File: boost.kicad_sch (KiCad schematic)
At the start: 41 parts, among them Q4 BSC059N04LS6, Q5 BSC059N04LS6, U17 LTC7804, U6 LTC7804

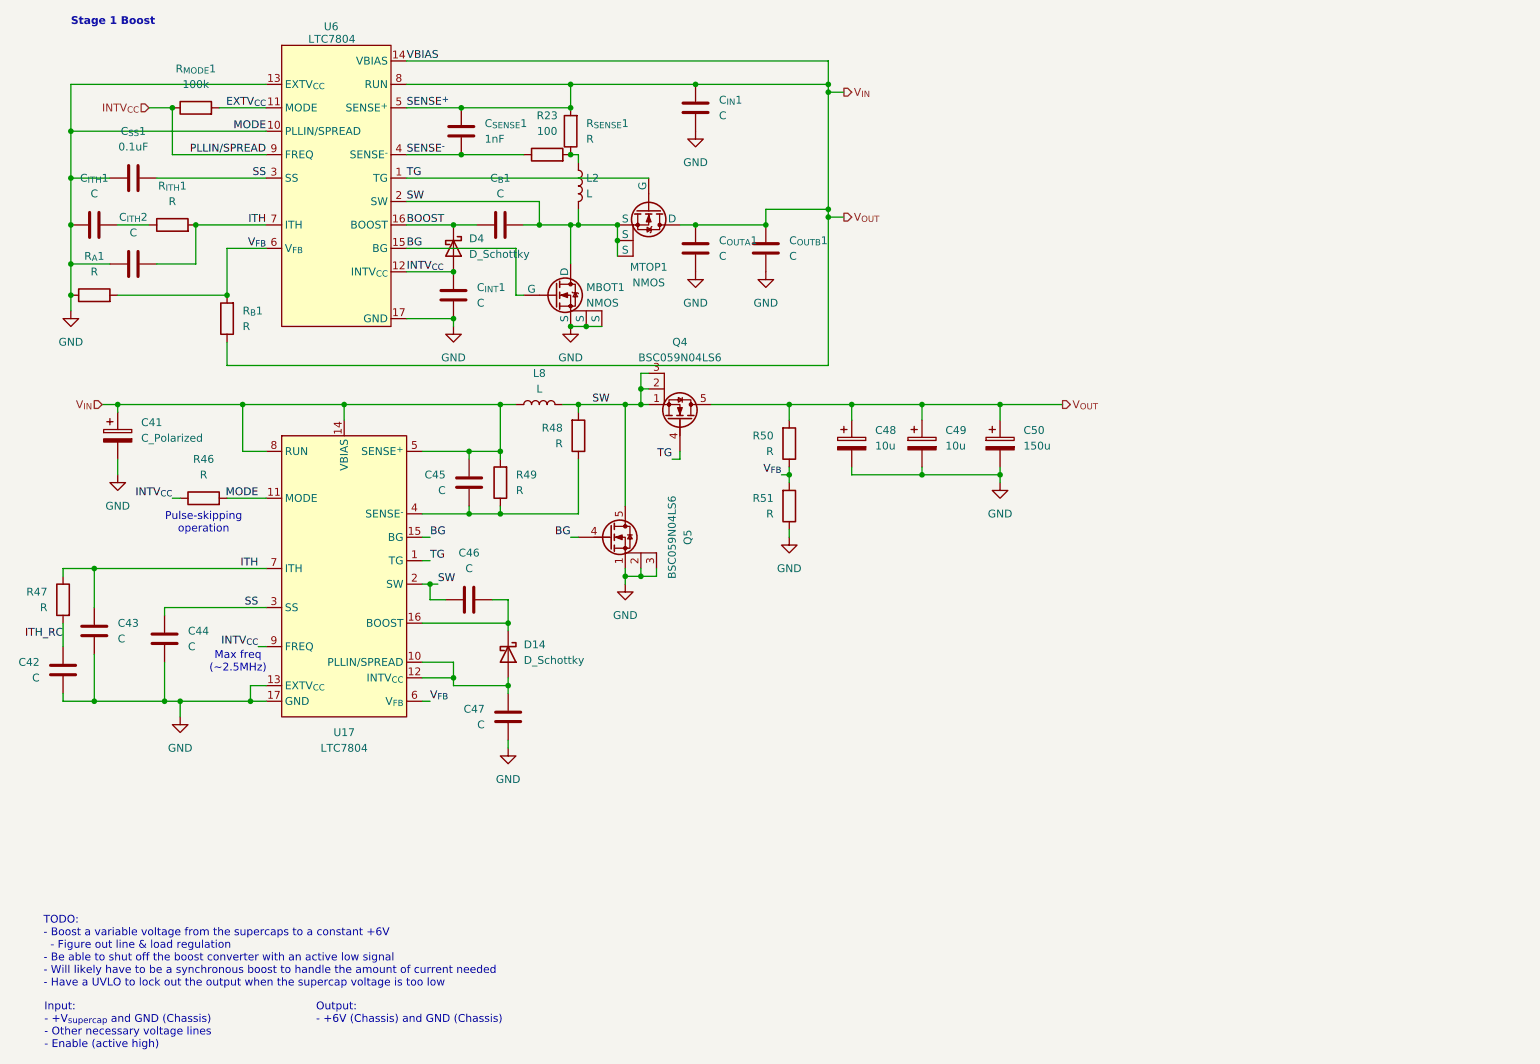
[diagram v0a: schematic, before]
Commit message: Redo boost converter (frist stage)
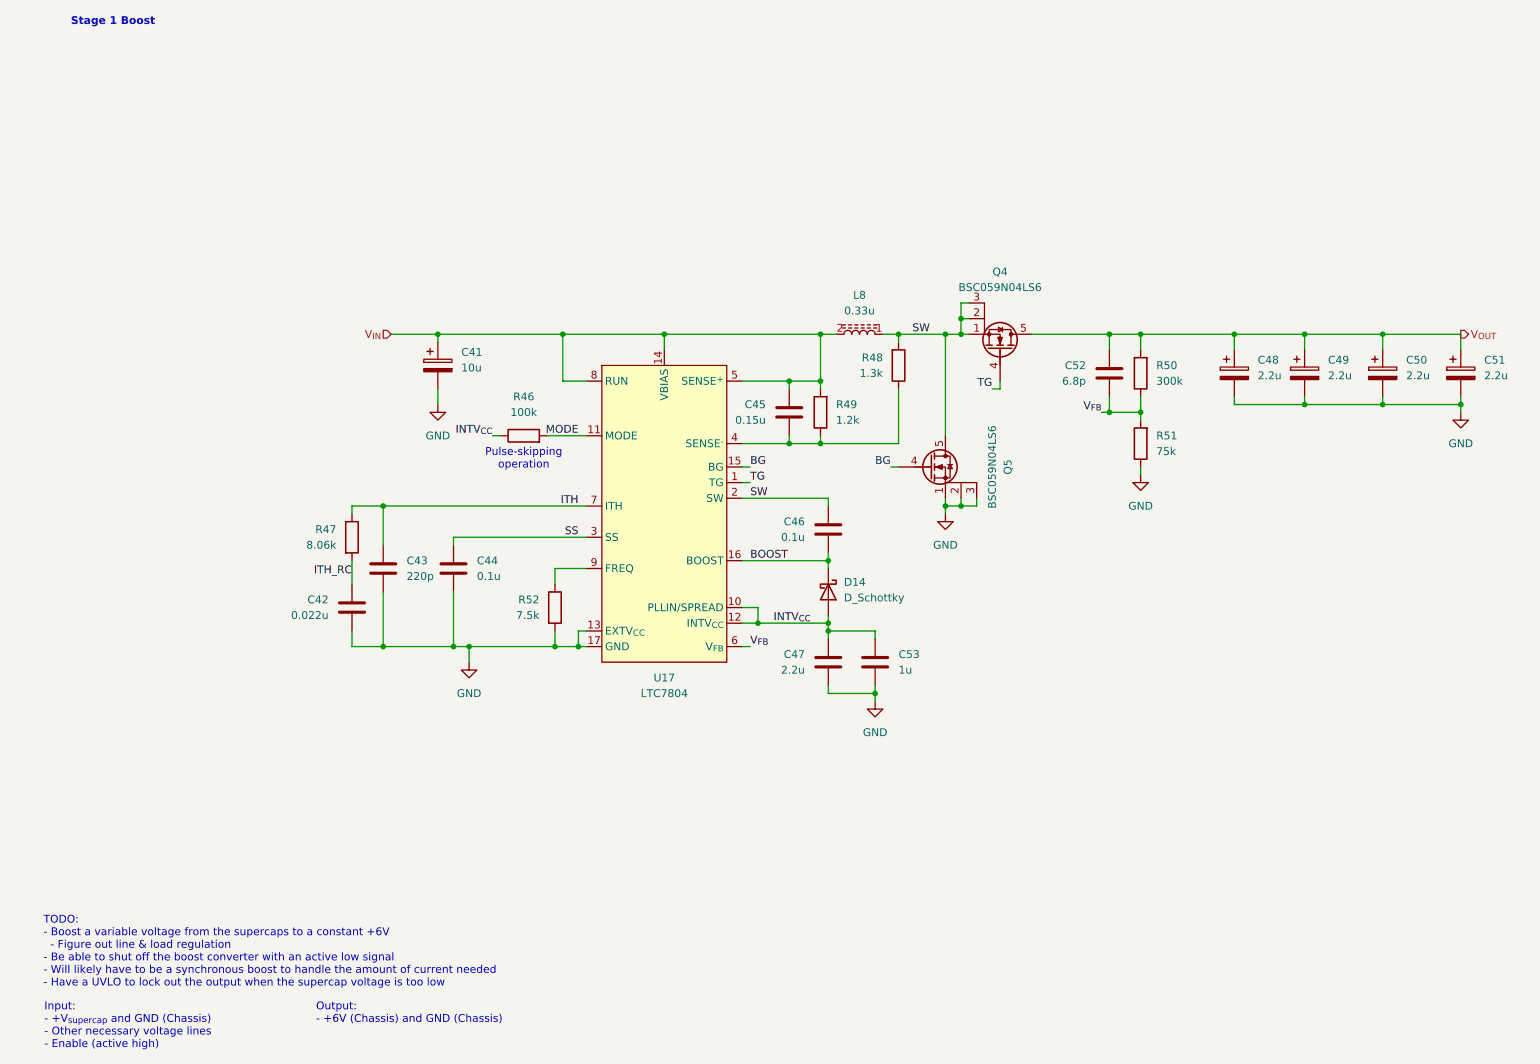
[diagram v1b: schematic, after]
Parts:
- removed C_{B}1, C_{INT}1, C_{IN}1, C_{ITH}1, C_{ITH}2, C_{OUTA}1, C_{OUTB}1: C, symbol Device:C
- removed C_{SENSE}1: 1nF, symbol Device:C
- removed C_{SS}1: 0.1uF, symbol Device:C
- removed D4: D_Schottky, symbol Device:D_Schottky
- removed L2: L, symbol Device:L
- removed MBOT1, MTOP1: NMOS, Package_SON:Infineon_PG-TDSON-8_6.15x5.15mm, symbol Simulation_SPICE:NMOS
- removed R23: 100, symbol Device:R
- removed R_{A}1, R_{B}1, R_{ITH}1, R_{SENSE}1: R, symbol Device:R
- removed R_{MODE}1: 100k, symbol Device:R
- removed U6: LTC7804, Package_DFN_QFN:QFN-16-1EP_3x3mm_P0.5mm_EP1.45x1.45mm, symbol ! Robomaster ICs:LTC7804
- added C51: 2.2u, Capacitor_THT:CP_Radial_D5.0mm_P2.00mm, symbol Device:C_Polarized
- added C52: 6.8p, Capacitor_SMD:C_0603_1608Metric_Pad1.08x0.95mm_HandSolder, symbol Device:C
- added C53: 1u, Capacitor_SMD:C_0603_1608Metric_Pad1.08x0.95mm_HandSolder, symbol Device:C
- added R52: 7.5k, Resistor_SMD:R_0603_1608Metric_Pad0.98x0.95mm_HandSolder, symbol Device:R
- C41: value C_Polarized -> 10u
- C42: value C -> 0.022u
- C43: value C -> 220p
- C44, C46: value C -> 0.1u
- C45: value C -> 0.15u
- C47: value C -> 2.2u
- C48, C49: value 10u -> 2.2u; footprint (none) -> Capacitor_THT:CP_Radial_D5.0mm_P2.00mm; Mouser Part Number (none) -> 710-860160672003
- C50: value 150u -> 2.2u; footprint (none) -> Capacitor_THT:CP_Radial_D5.0mm_P2.00mm; Mouser Part Number (none) -> 710-860160672003
- L8: value L -> 0.33u; footprint (none) -> Inductor_SMD:L_Bourns_SRP7028A_7.3x6.6mm; symbol Device:L -> Device:L_Ferrite; Mouser Part Number (none) -> 652-SRP7028A-R33M
- R46: value R -> 100k
- R47: value R -> 8.06k
- R48: value R -> 1.3k
- R49: value R -> 1.2k
- R50: value R -> 300k
- R51: value R -> 75k
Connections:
- net BOOST: now also C46.2, D14.1 (K), U17.16 (BOOST)
- net GND: now also C51.2, C53.2, R52.2; no longer R46.2, U17.11 (MODE)
- net INTV_{CC}: now also C47.1, D14.2 (A), U17.10 (PLLIN/SPREAD), U17.12 (INTV_{CC}), C53.1; no longer U17.9 (FREQ)
- net SW: now also L8.1; no longer L8.2
- net V_{FB}: now also C52.2
- net V_{IN}: now also L8.2; no longer C48.1, C49.1, C50.1, L8.1, Q4.5 (D), R50.2
- new net: R52.1, U17.9 (FREQ)
- new net MODE: R46.2, U17.11 (MODE)
- new net V_{OUT}: C48.1, C49.1, C50.1, C51.1, C52.1, Q4.5 (D), R50.2
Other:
- note removed: "Max freq (~2.5MHz)"
- moved on the sheet: C41, C42, C43, C44, C45, C47, C48, D14, Q4, Q5, R46, R47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

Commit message: Correct symbol library path, renumber components
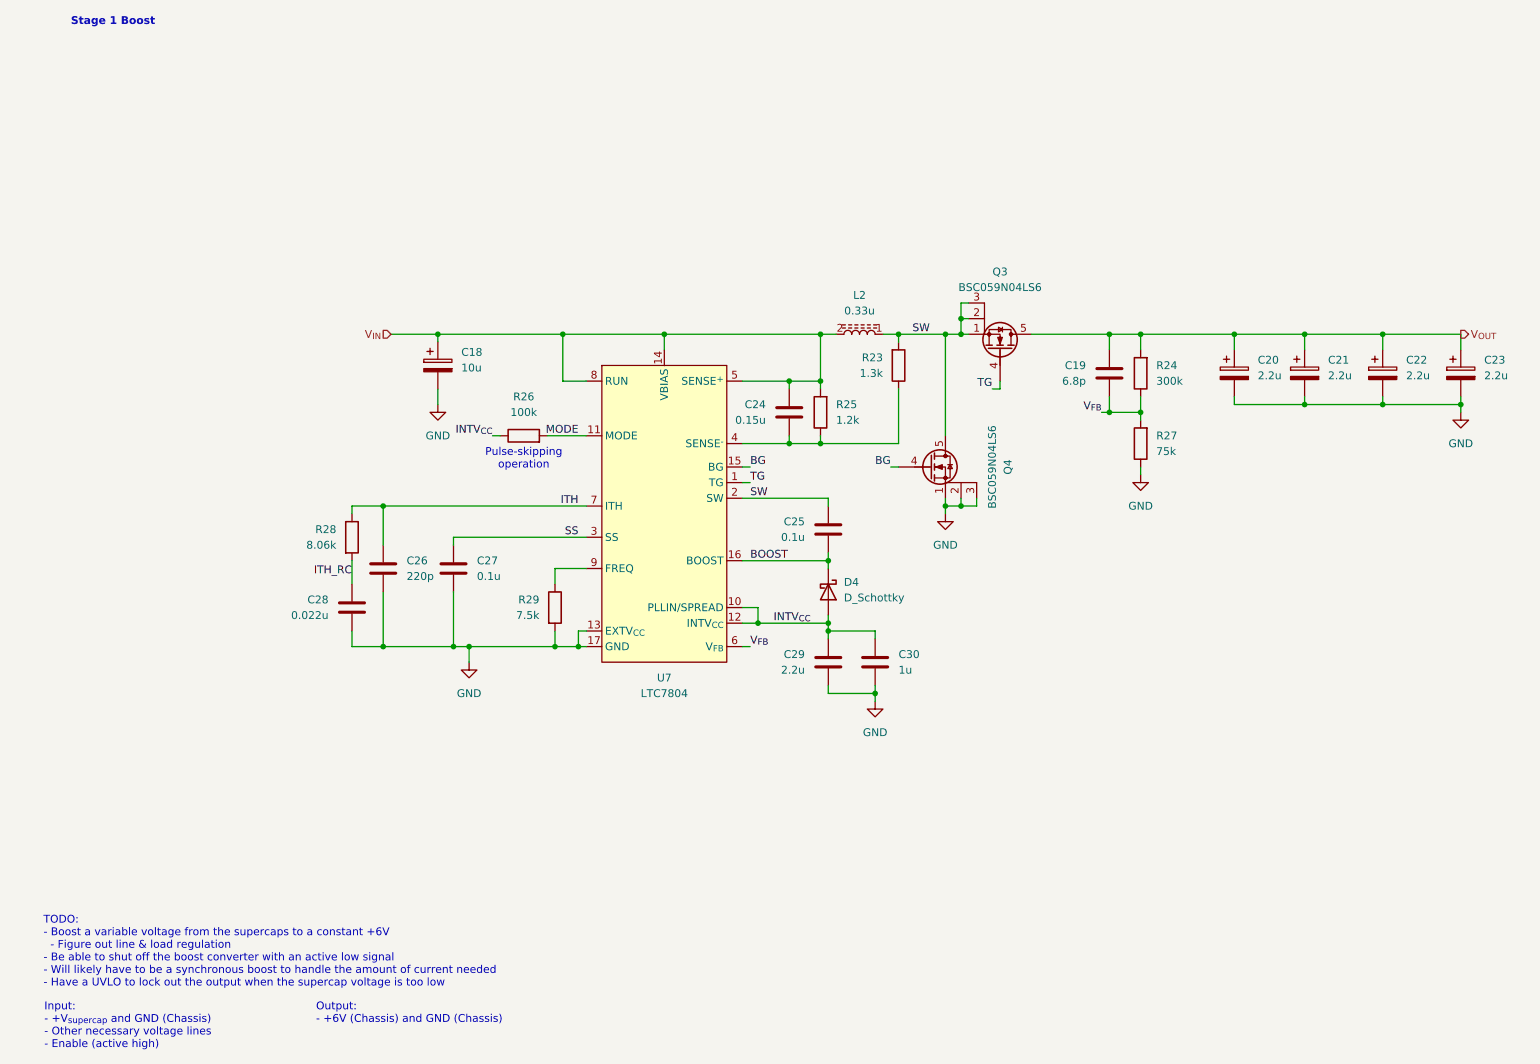
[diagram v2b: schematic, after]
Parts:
- renumbered C41 to C18, C52 to C19, C48 to C20, C49 to C21, C50 to C22, C51 to C23, C45 to C24, C46 to C25, C43 to C26, C44 to C27, C42 to C28, C47 to C29, C53 to C30, D14 to D4, L8 to L2, Q4 to Q3, Q5 to Q4, R48 to R23, R50 to R24, R49 to R25, R46 to R26, R51 to R27, R47 to R28, R52 to R29, U17 to U7

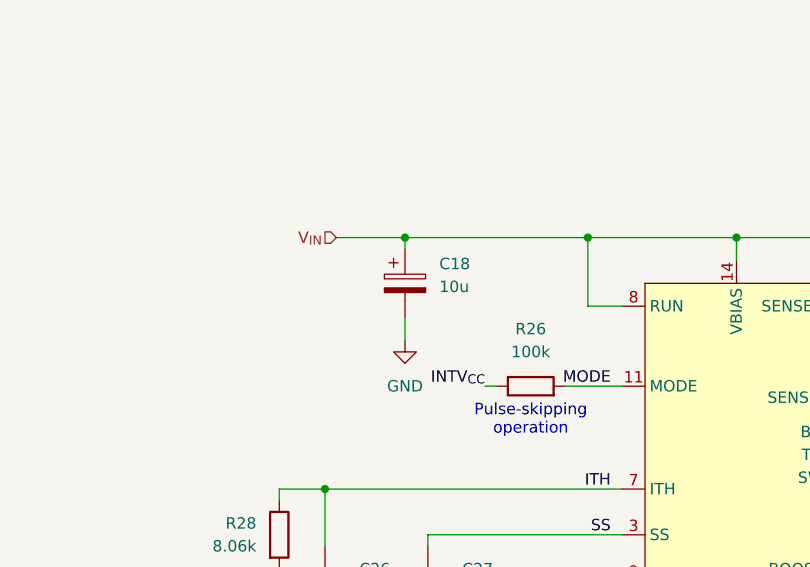
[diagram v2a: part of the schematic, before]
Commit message: Add new components to housekeeping power supply
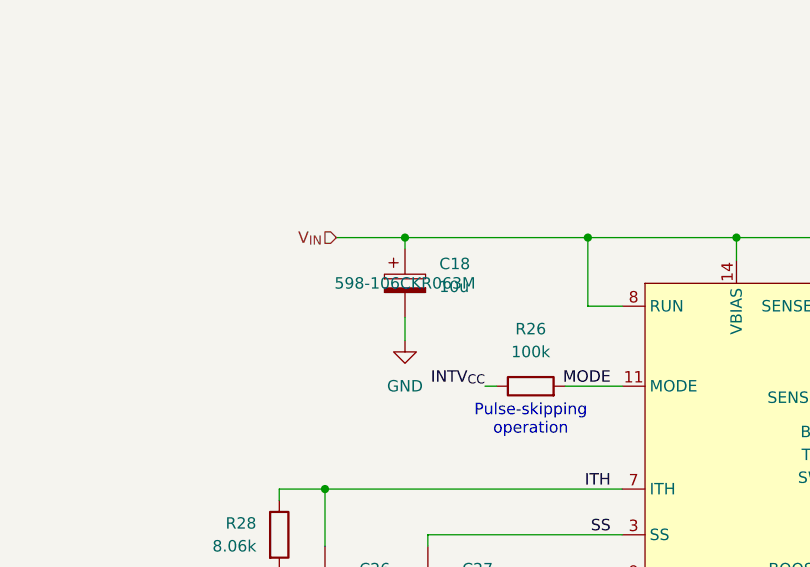
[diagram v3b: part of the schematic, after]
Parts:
- C18: footprint (none) -> Capacitor_THT:CP_Radial_D5.0mm_P2.00mm; Mouser Part Number (none) -> 598-106CKR063M

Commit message: Redesign housekeeping supplies
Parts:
- removed D4: D_Schottky, symbol Device:D_Schottky
- added D15: BAT54, Package_TO_SOT_SMD:SOT-23_Handsoldering, symbol Device:D_Schottky
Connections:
- net BOOST: now also D15.3 (K)
- net INTV_{CC}: now also D15.1 (A)
- net V_{IN}: no longer U7.14 (VBIAS)
- new net +5V: U7.14 (VBIAS)
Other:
- moved on the sheet: C19, C20, C21, C22, C23, L2, Q3, R24, R27

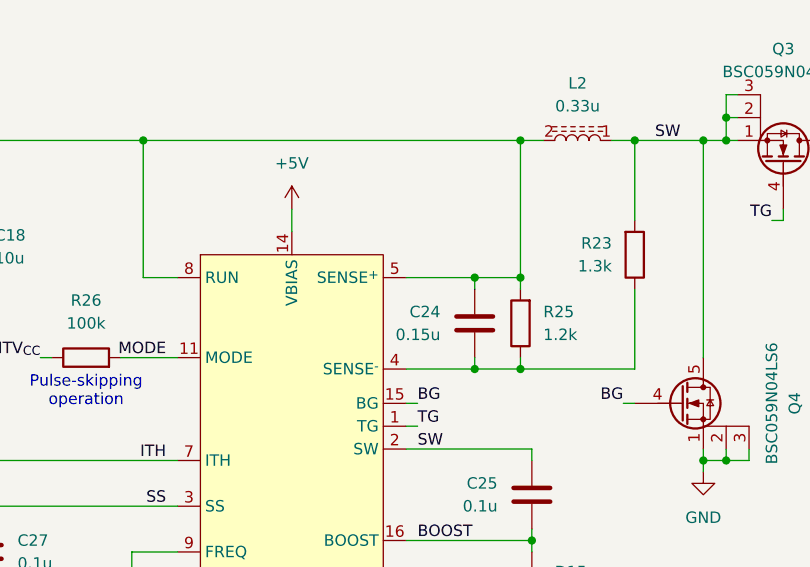
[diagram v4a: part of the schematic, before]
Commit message: Update Mouser part numbers
Some resistors will be wrong, please check
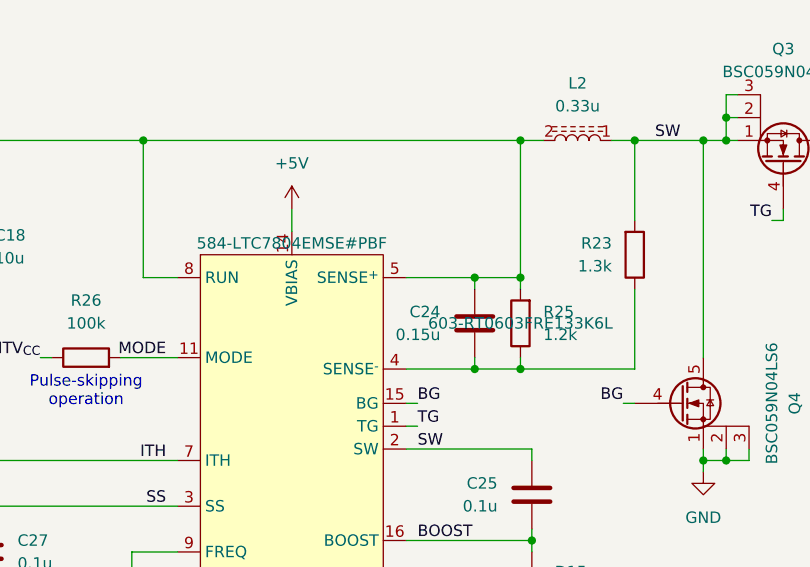
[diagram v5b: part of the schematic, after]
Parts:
- C30: Mouser Part Number (none) -> 80-C0603C105K9PLR
- R25: Mouser Part Number (none) -> 603-RT0603FRE133K6L
- U7: Mouser Part Number (none) -> 584-LTC7804EMSE#PBF
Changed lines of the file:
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@@
+			)
+		)
+		(property "Mouser Part Number" "584-LTC7804EMSE#PBF"
+			(at 120.65 78.74 0)
+			(effects
+				(font
+					(size 1.27 1.27)
+				)
 			)
 		)
@@
 					(size 1.27 1.27)
 				)
+			)
+		)
+		(property "Mouser Part Number" "80-C0603C105K9PLR"
+			(at 154.94 128.27 0)
+			(effects
+				(font
+					(size 1.27 1.27)
+				)
+				(hide yes)
 			)
 		)
@@
 			(at 146.05 87.63 0)
 			(effects
+				(font
+					(size 1.27 1.27)
+				)
+			)
+		)
+		(property "Mouser Part Number" "603-RT0603FRE133K6L"
+			(at 146.05 87.63 0)
+			(effects
